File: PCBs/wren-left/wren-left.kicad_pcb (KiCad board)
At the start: 2 copper layers, 228.6 x 115.2 mm, 102 parts, among them J1 TRRS_Jack, SW0 Reset, U1 Elite-C

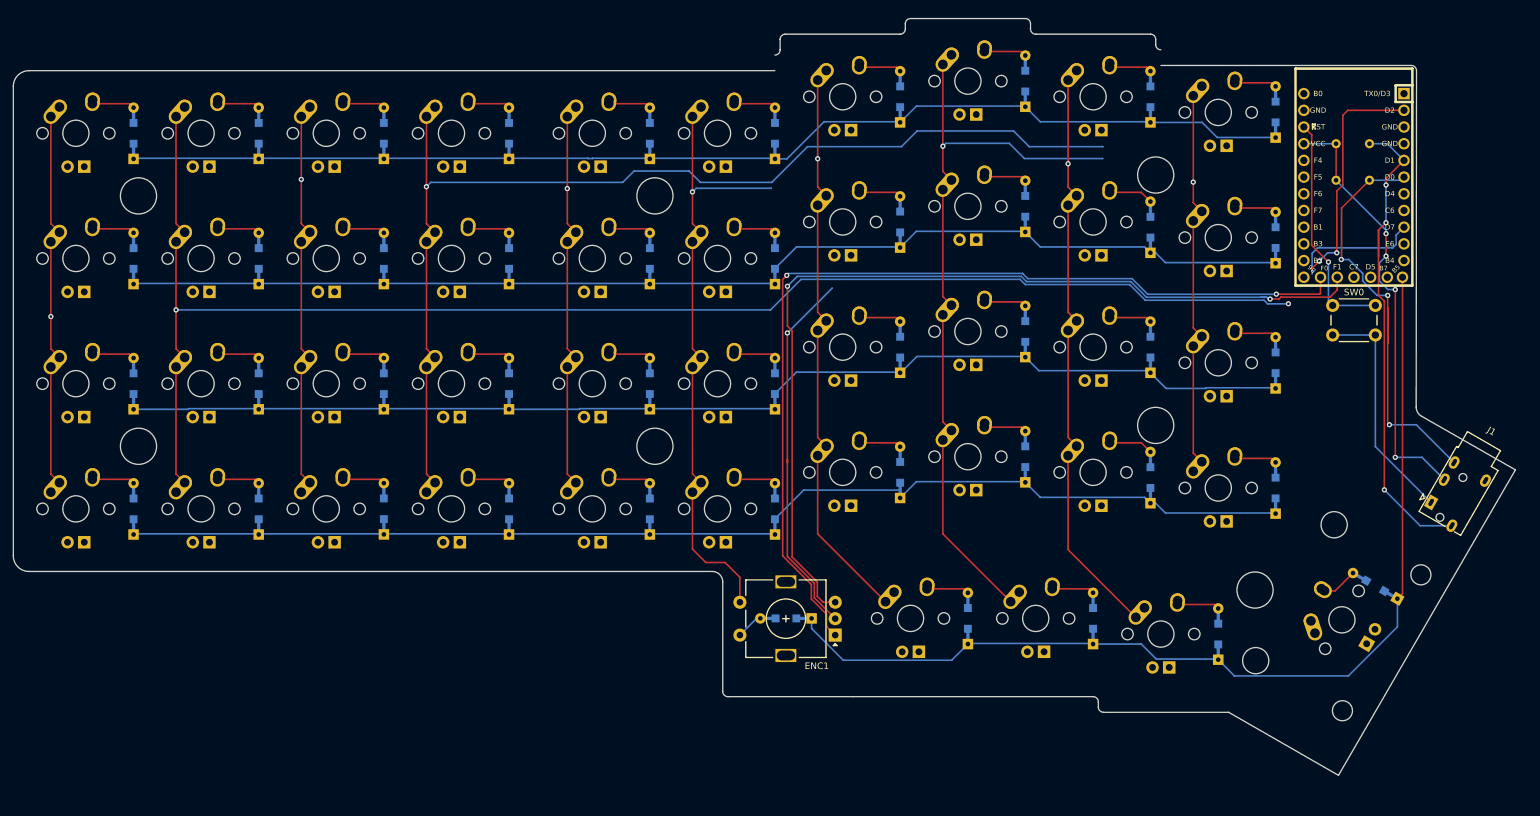
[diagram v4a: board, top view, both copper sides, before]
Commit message: Finish left side kyria-like stagger
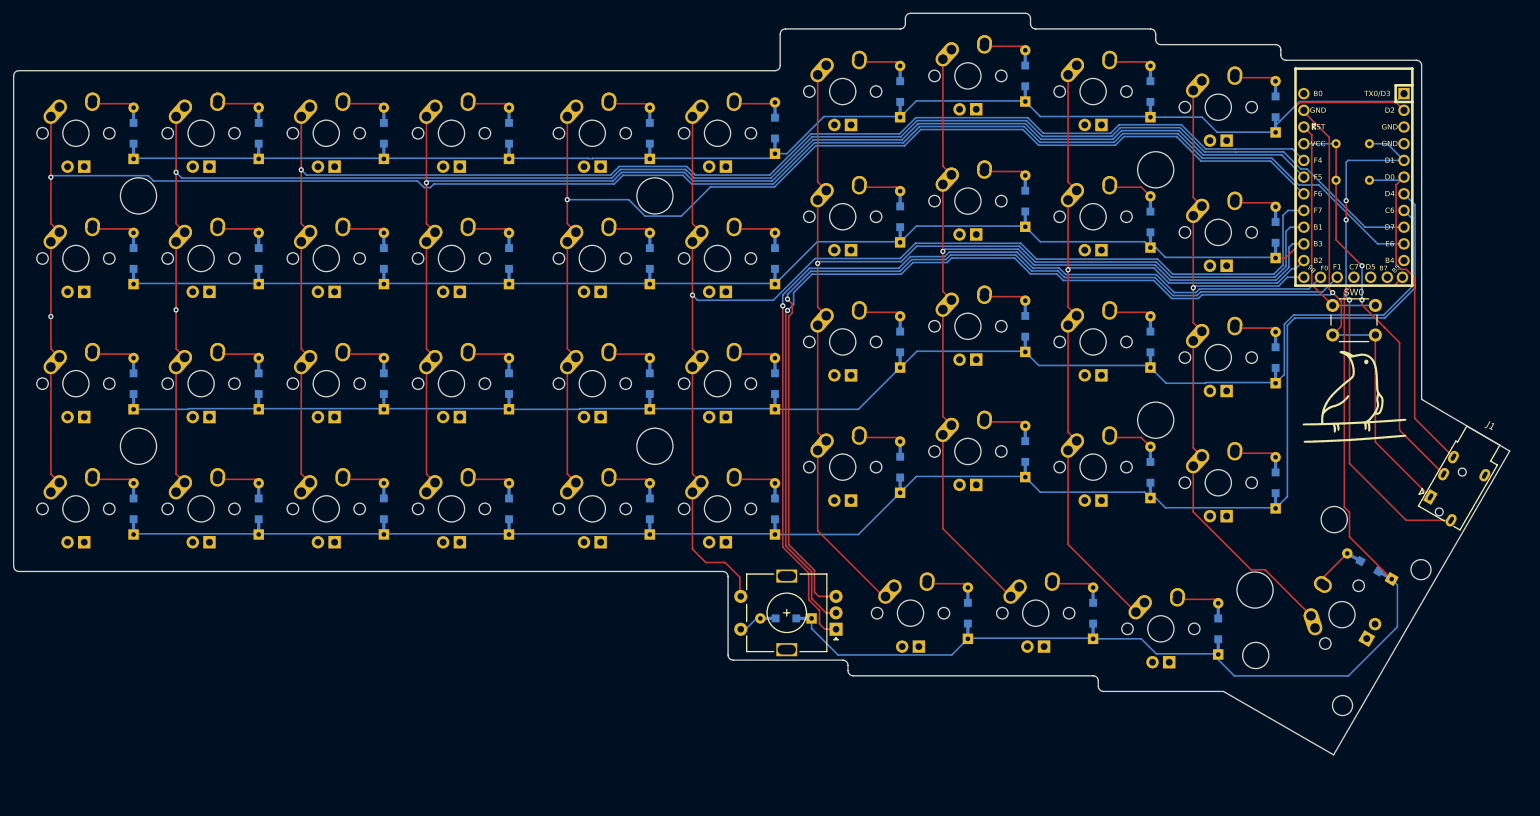
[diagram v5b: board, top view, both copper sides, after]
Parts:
- added G***: LOGO, footprints:wren_logo, F.Cu at (241.4, 76.6)
- moved D41 3.11 mm to (243.7, 102.4)
- moved ENC1 0.90 mm to (162.5, 112.0)
- moved J1 0.83 mm to (252.9, 91.9)
- moved D11 0.79 mm to (229.4, 51.6)
- moved D13 0.79 mm to (191.3, 46.8)
- moved D14 0.79 mm to (172.2, 49.2)
- moved D21 0.79 mm to (229.4, 70.6)
- moved D22 0.79 mm to (210.3, 68.3)
- moved D23 0.79 mm to (191.3, 65.9)
- moved D24 0.79 mm to (172.2, 68.3)
- moved D31 0.79 mm to (229.4, 89.7)
- moved D32 0.79 mm to (210.3, 88.1)
- moved D34 0.79 mm to (172.2, 87.3)
- moved D42 0.79 mm to (220.7, 111.9)
- moved D43 0.79 mm to (201.6, 109.5)
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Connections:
- U1 pad 7: ROW2 -> ROW3
- U1 pad 8: ROW3 -> ROW2
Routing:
- net COL9: track 54.4 -> 274.6 mm, vias 1 -> 2
- net COL7: track 54.4 -> 215.8 mm
- net COL5: track 54.4 -> 178.1 mm
- net GND: track 92.1 -> 213.0 mm, vias 1 -> 2
- net COL4: track 88.1 -> 183.2 mm
- net COL3: track 80.9 -> 164.3 mm
- net ROW3: track 179.2 -> 245.2 mm
- net COL0: track 54.4 -> 103.3 mm
- net ROW2: track 178.5 -> 223.2 mm
- net COL1: track 83.3 -> 121.6 mm
- net COL2: track 108.7 -> 144.4 mm
- net COL6: track 163.6 -> 197.6 mm
- net ROW0: track 179.3 -> 201.9 mm
- net SCL: track 66.7 -> 52.6 mm, vias 3 -> 0
- net ROW4: track 152.4 -> 162.6 mm
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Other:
- board size 228.6 x 115.2 mm -> 227.7 x 112.8 mm

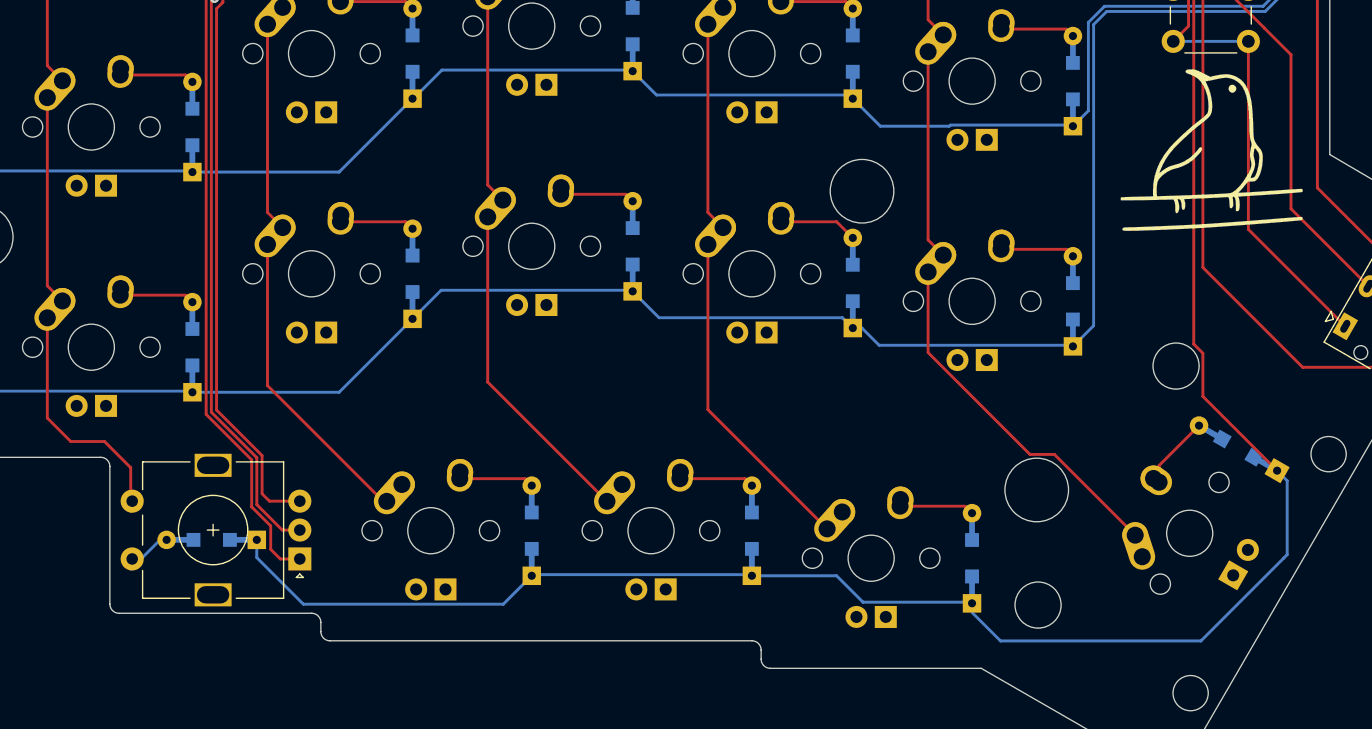
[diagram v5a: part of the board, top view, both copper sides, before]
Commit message: Finalize encoder position on left side
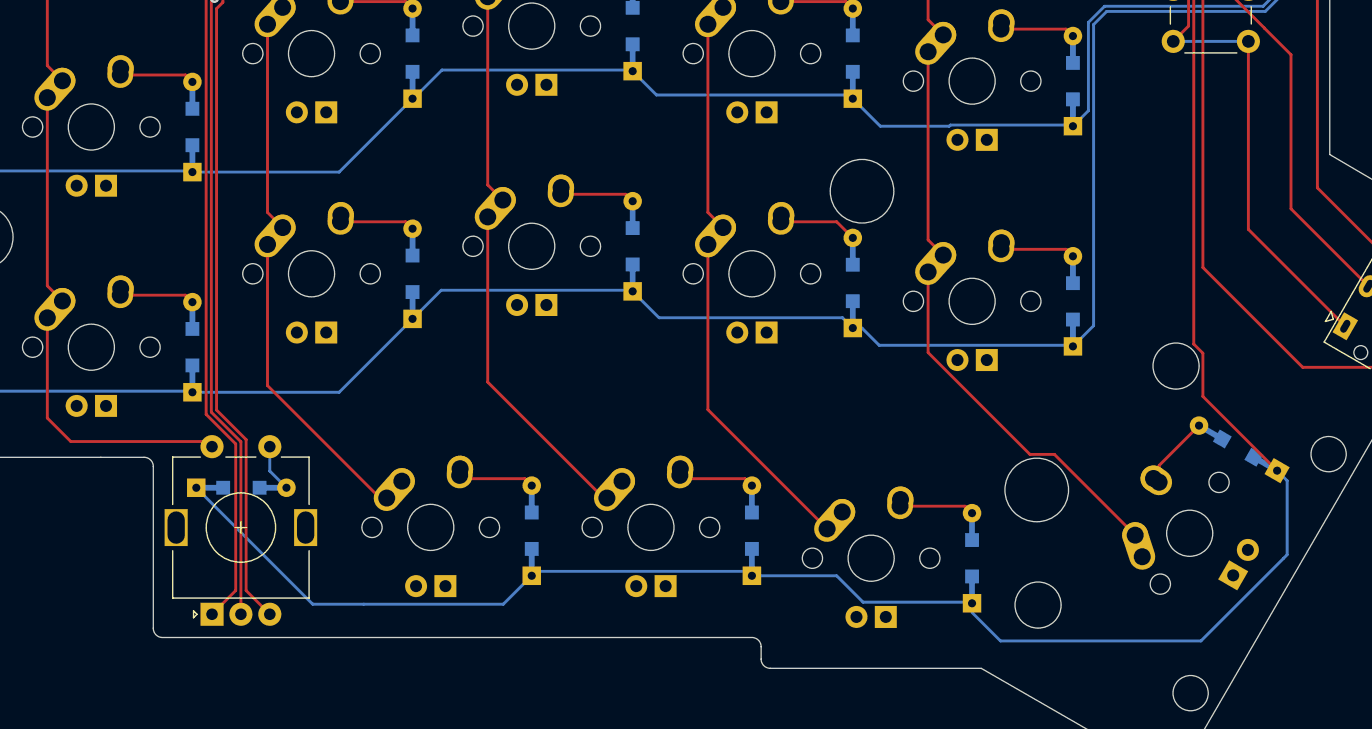
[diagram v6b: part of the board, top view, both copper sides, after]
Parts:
- removed G***: LOGO, footprints:wren_logo
- moved ENC1 8.98 mm to (154.9, 116.8), turned to 90 degrees
- moved D45 5.19 mm to (157.4, 105.8), turned to 0 degrees
- moved MX44 0.29 mm to (173.8, 109.3)
- moved MX43 0.29 mm to (192.9, 109.3)
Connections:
- ENC1 pad S1: COL4 -> ENC1-IN
- ENC1 pad S2: ENC1-IN -> COL4
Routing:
- net RIGHT: track 140.9 -> 148.0 mm
- net ROW4: track 162.6 -> 169.0 mm
- net GND: track 213.0 -> 217.6 mm
- net COL4: track 183.2 -> 185.7 mm
- net LEFT: track 143.3 -> 145.7 mm
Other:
- outline, holes or cut-outs redrawn

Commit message: Add increased stagger to right side
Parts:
- added G***: LOGO, footprints:wren_logo, F.Cu at (241.3, 76.9)
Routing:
- net SDA: track 80.3 -> 77.7 mm
